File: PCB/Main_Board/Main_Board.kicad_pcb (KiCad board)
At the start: 2 copper layers, 86.9 x 90.9 mm, 26 parts, among them J1 ESP32_Left, J2 ESP32_Right, J3 POWER_SUPPLY, J4 BUCK_IN, J5 BUCK_OUT, J6 CABLE, J7 MOTOR, J8 LIMIT_SWITCH, J9 ToF

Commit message: Minor fixes
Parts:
- J8: renamed from J6; footprint Connector_JST:JST_PH_B8B-PH-K_1x08_P2.00mm_Vertical -> Connector_JST:JST_XH_B8B-XH-A_1x08_P2.50mm_Vertical
- J9: renamed from J7; footprint Connector_JST:JST_PH_B8B-PH-K_1x08_P2.00mm_Vertical -> Connector_JST:JST_XH_B8B-XH-A_1x08_P2.50mm_Vertical
- moved C4 3.81 mm to (78.8, 44.5)
- moved C5 3.81 mm to (90.2, 44.5)
- moved R8 2.54 mm to (86.4, 80.0)
- renumbered C5 to C2, C4 to C3, C3 to C4, C2 to C5, H4 to H1, H3 to H2, H2 to H3, H1 to H4, J3 to J1, J8 to J2, J9 to J3, J1 to J6, J2 to J7, R8 to R1, R5 to R2, R6 to R3, R3 to R4, R4 to R5, R7 to R6, R1 to R7, R2 to R8
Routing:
- net Net-(J8-Pin_7): track 13.1 -> 18.9 mm
- net Net-(J9-Pin_7): track 19.7 -> 23.0 mm
- net /IS_R: track 46.9 -> 50.0 mm
- net Net-(J8-Pin_8): track 23.6 -> 25.9 mm
- net Net-(J8-Pin_4): track 19.8 -> 21.3 mm
- net Net-(J8-Pin_3): track 22.3 -> 23.6 mm
- net Net-(J8-Pin_5): track 7.80 -> 8.89 mm
- net /IS_L: track 53.3 -> 54.4 mm
- net /DISP_RST: track 51.3 -> 50.3 mm
- net Net-(J9-Pin_8): track 8.63 -> 7.82 mm
- net /3V3: track 115.6 -> 114.9 mm
- net /EN_L: track 17.0 -> 17.6 mm
- net /EN_R: track 16.6 -> 17.2 mm
- net /PWM_L: track 17.2 -> 16.7 mm
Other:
- board text added: "ESP32-S3 Meow"

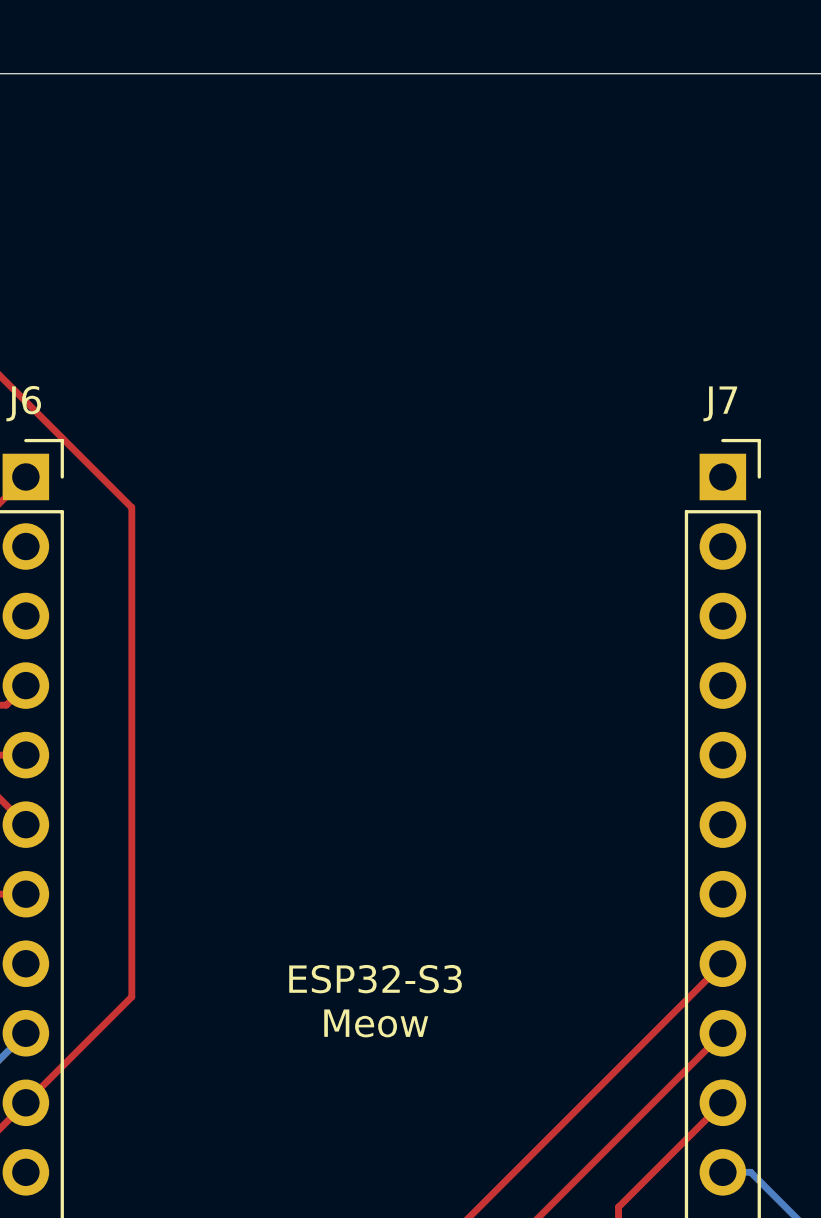
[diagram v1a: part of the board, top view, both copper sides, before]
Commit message: Added UI board Cosmetics in main board
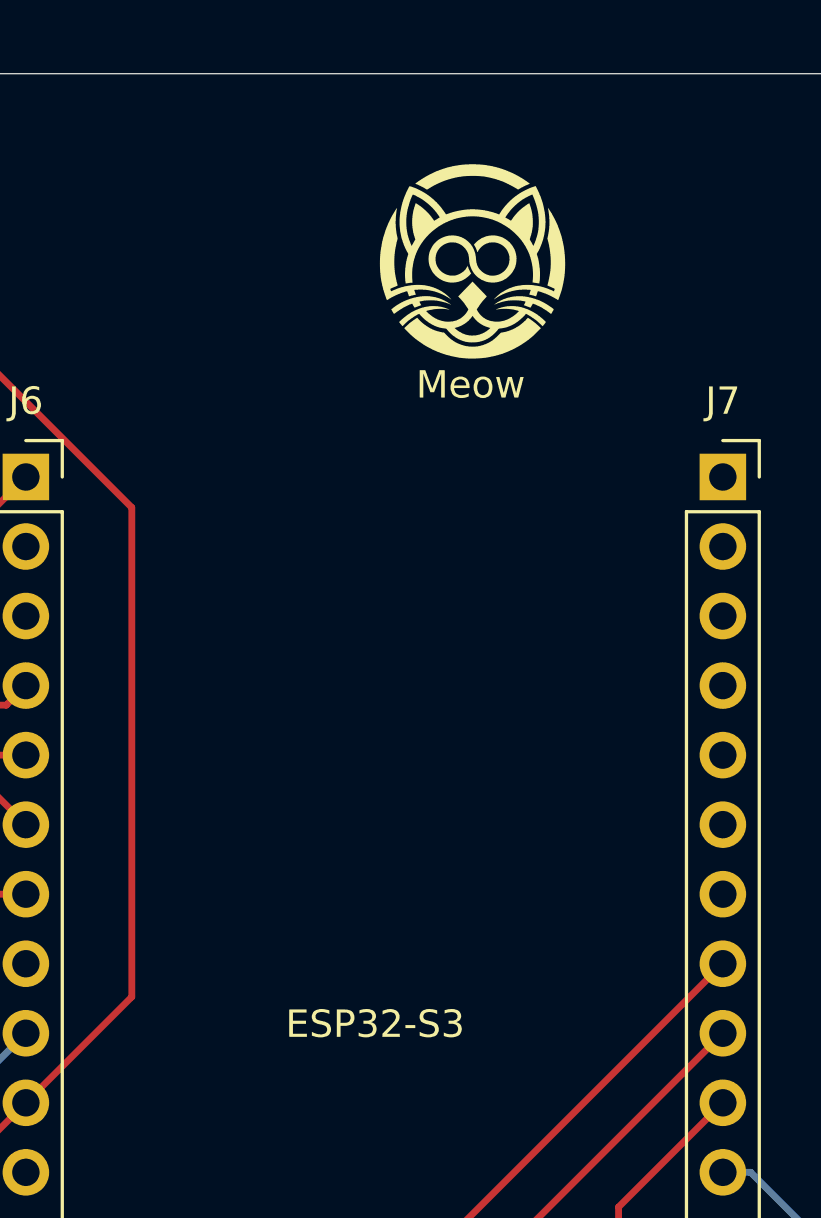
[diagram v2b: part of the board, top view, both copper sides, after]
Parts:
- added ?: , clipboard:13b59317-ab6f-4fc0-bdb4-4b3abb5c9487, F.Cu at (118.2, 43.4)
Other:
- board text added: "ESP32-S3"
- board text added: "Meow"
- board text removed: "ESP32-S3 Meow"

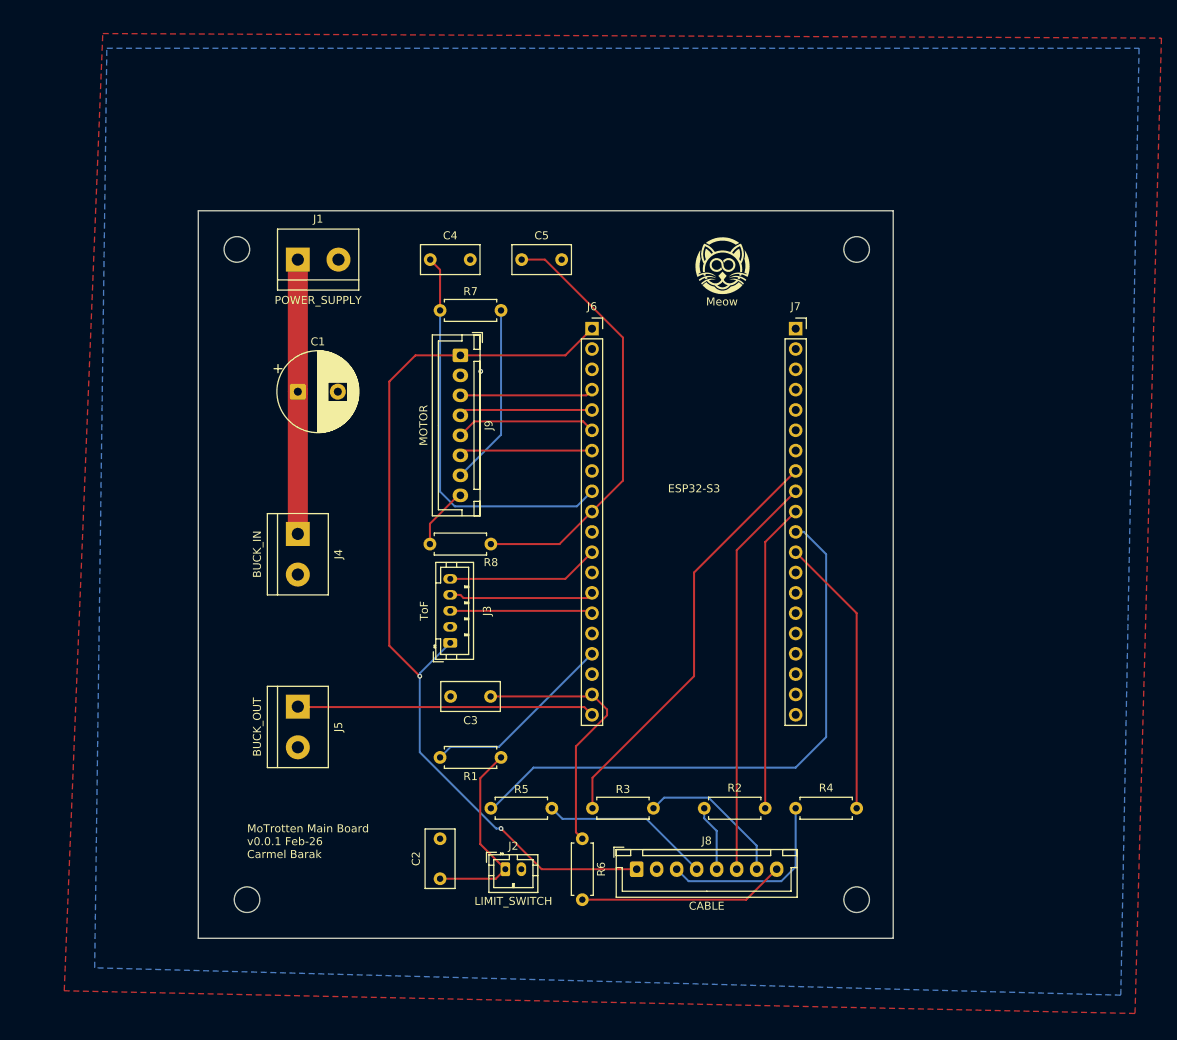
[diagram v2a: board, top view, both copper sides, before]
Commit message: Cleanup main board + fixed GPIOs used
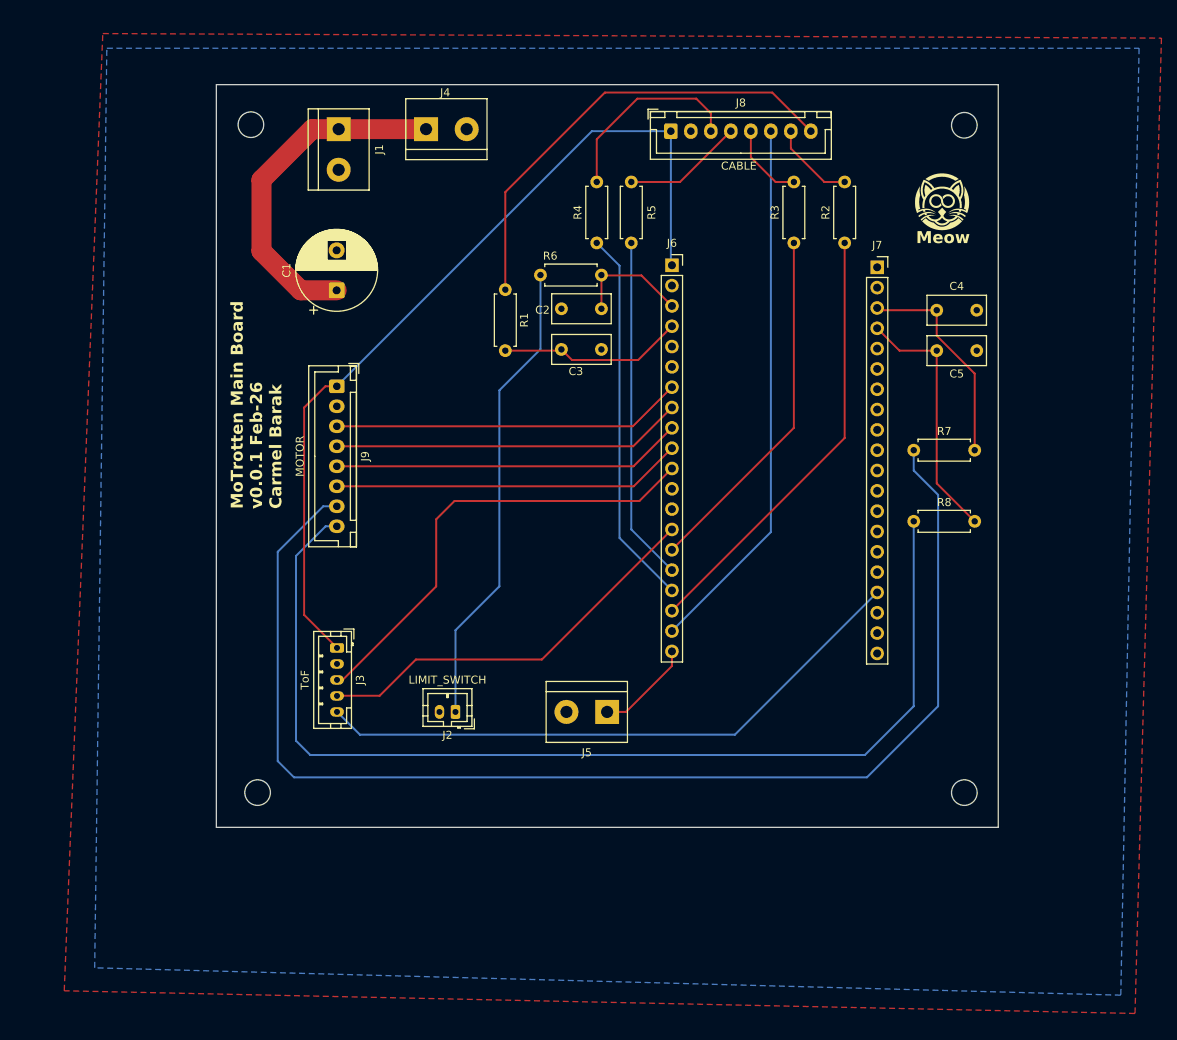
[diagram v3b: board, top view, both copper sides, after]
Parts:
- moved H2 131.9 mm to (145.5, 27.7)
- moved H1 123.0 mm to (56.4, 27.6)
- moved H3 113.5 mm to (145.5, 111.1)
- moved H4 101.1 mm to (57.2, 111.1)
- moved J8 92.4 mm to (108.9, 28.4)
- moved R4 77.8 mm to (99.6, 42.4), turned to 90 degrees
- moved R3 75.0 mm to (124.2, 42.4), turned to 90 degrees
- moved R5 72.8 mm to (103.9, 42.4), turned to 90 degrees
- moved R2 71.4 mm to (130.6, 42.4), turned to 90 degrees
- moved R6 70.7 mm to (92.6, 46.4), turned to 0 degrees
- moved C2 67.9 mm to (95.2, 55.7), turned to 0 degrees
- moved C4 63.6 mm to (142.1, 50.8)
- moved R7 61.7 mm to (139.2, 68.3)
- moved R1 58.5 mm to (88.2, 48.2), turned to -90 degrees
- moved C5 53.1 mm to (142.1, 55.8)
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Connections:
- net Net-(J8-Pin_3) renamed /CLK
- net Net-(J8-Pin_4) renamed /MOSI
- C2 pad 1: /LIMIT_SW -> Net-(J6-Pin_4)
- C3 pad 1: /BTNS -> Net-(J6-Pin_3)
- C4 pad 1: /IS_R -> Net-(J7-Pin_3)
- C5 pad 1: /IS_L -> Net-(J7-Pin_4)
- J6 pad 10: /IS_L -> /EN_L
- J6 pad 11: unconnected-(J6-Pin_11-Pad11) -> /I2C_SDA
- J6 pad 12: /XSHUT -> unconnected-(J6-Pin_12-Pad12)
- J6 pad 15: /I2C_SDA -> /DISP_CS
- J6 pad 16: unconnected-(J6-Pin_16-Pad16) -> /DISP_MOSI
- J6 pad 17: Net-(J6-Pin_17) -> /DISP_CLK
- J6 pad 18: unconnected-(J6-Pin_18-Pad18) -> /DISP_DC
- J6 pad 19: /BTNS -> /DISP_RST
- J6 pad 3: unconnected-(J6-Pin_3-Pad3) -> Net-(J6-Pin_3)
- J6 pad 4: /EN_R -> Net-(J6-Pin_4)
- J6 pad 5: /PWM_R -> unconnected-(J6-Pin_5-Pad5)
- J6 pad 6: /EN_L -> unconnected-(J6-Pin_6-Pad6)
- J6 pad 7: /PWM_L -> /PWM_R
- J6 pad 8: unconnected-(J6-Pin_8-Pad8) -> /PWM_L
- J6 pad 9: /IS_R -> /EN_R
- J7 pad 10: /DISP_DC -> unconnected-(J7-Pin_10-Pad10)
- J7 pad 11: /DISP_CLK -> unconnected-(J7-Pin_11-Pad11)
- J7 pad 12: /DISP_MOSI -> unconnected-(J7-Pin_12-Pad12)
- J7 pad 17: unconnected-(J7-Pin_17-Pad17) -> /XSHUT
- J7 pad 3: unconnected-(J7-Pin_3-Pad3) -> Net-(J7-Pin_3)
- J7 pad 4: unconnected-(J7-Pin_4-Pad4) -> Net-(J7-Pin_4)
- J7 pad 8: /DISP_CS -> unconnected-(J7-Pin_8-Pad8)
- J7 pad 9: /DISP_RST -> unconnected-(J7-Pin_9-Pad9)
- J8 pad 5: Net-(J8-Pin_5) -> /CS
- J8 pad 7: Net-(J8-Pin_7) -> /DC
- J8 pad 8: Net-(J8-Pin_8) -> /BTNS
- J9 pad 3: /EN_R -> /PWM_R
- J9 pad 4: /PWM_R -> /PWM_L
- J9 pad 5: /EN_L -> /EN_R
- J9 pad 6: /PWM_L -> /EN_L
- J9 pad 7: Net-(J9-Pin_7) -> /IS_R
- J9 pad 8: Net-(J9-Pin_8) -> /IS_L
- R1 pad 1: /LIMIT_SW -> /BTNS
- R1 pad 2: Net-(J6-Pin_17) -> Net-(J6-Pin_4)
- R2 pad 2: Net-(J8-Pin_5) -> /DC
- R3 pad 2: Net-(J8-Pin_7) -> /CS
- R4 pad 1: /DISP_MOSI -> /DISP_CLK
- R5 pad 1: /DISP_CLK -> /DISP_MOSI
- R6 pad 1: /BTNS -> /LIMIT_SW
- R6 pad 2: Net-(J8-Pin_8) -> Net-(J6-Pin_3)
- R7 pad 2: Net-(J9-Pin_7) -> Net-(J7-Pin_3)
- R8 pad 2: Net-(J9-Pin_8) -> Net-(J7-Pin_4)
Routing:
- net /IS_R: track 50.0 -> 156.2 mm
- net /IS_L: track 54.4 -> 133.3 mm
- net /XSHUT: track 19.1 -> 76.1 mm
- net /I2C_SDA: track 17.8 -> 57.7 mm
- net /LIMIT_SW: track 25.0 -> 59.0 mm
- net /I2C_SCL: track 17.9 -> 50.5 mm
- net Net-(J7-Pin_4): track 0.00 -> 31.9 mm
- net /PWM_L: track 16.7 -> 43.9 mm
- net /PWM_R: track 16.7 -> 43.9 mm
- net Net-(J7-Pin_3): track 0.00 -> 27.0 mm
- net /EN_R: track 17.2 -> 43.9 mm
- net /EN_L: track 17.6 -> 43.9 mm
- net /DISP_CLK: track 73.5 -> 47.3 mm
- net Net-(J8-Pin_8): track 25.9 -> 0.00 mm
- net /+5V: track 37.2 -> 12.3 mm
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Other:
- board size 86.9 x 90.9 mm -> 97.7 x 92.8 mm
- board text removed: "ESP32-S3"

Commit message: Added fuse + cleanups
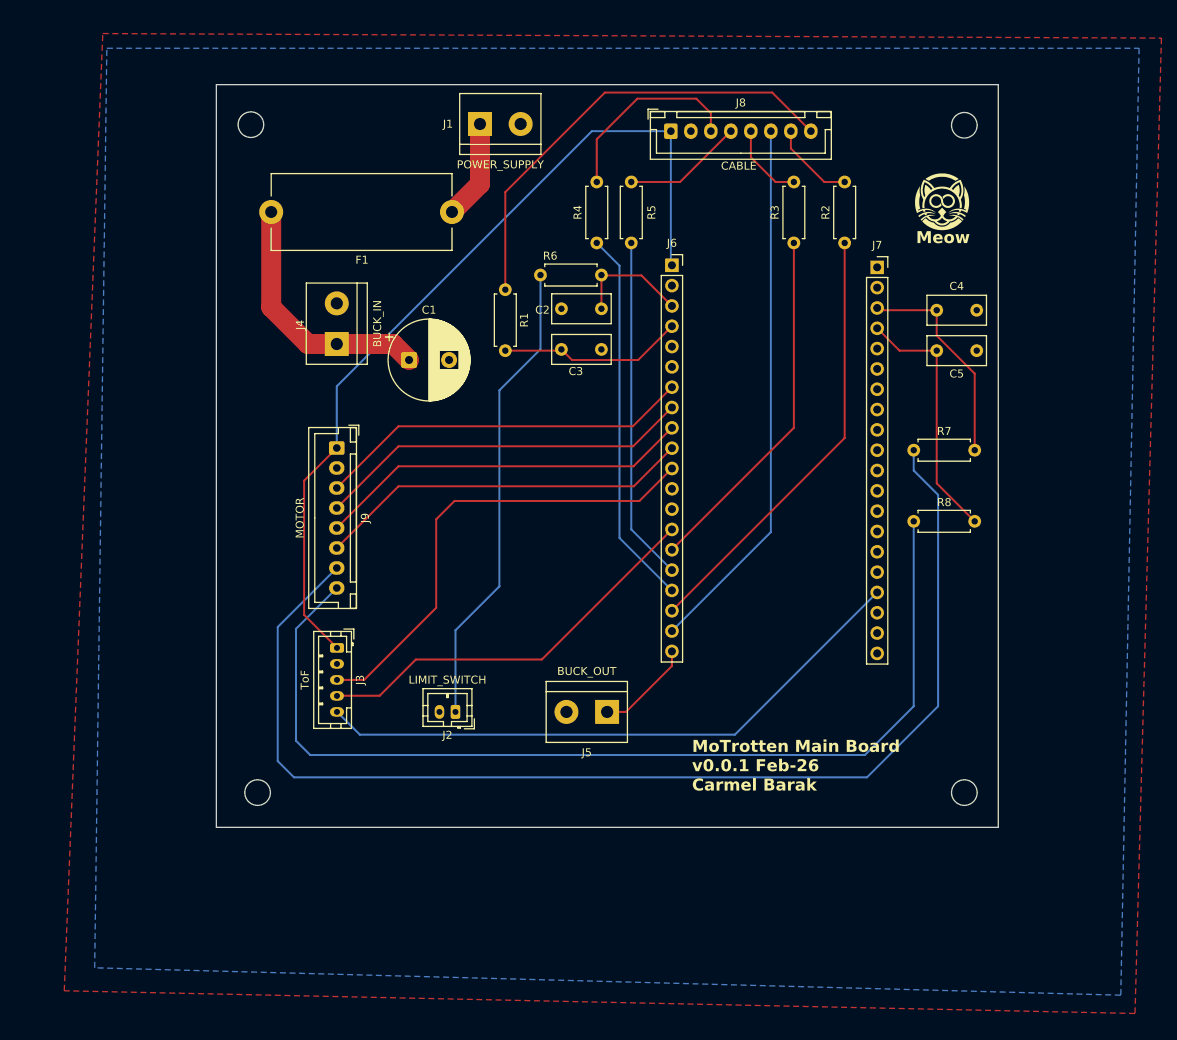
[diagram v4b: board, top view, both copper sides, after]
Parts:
- added F1: Fuse, Fuse:Fuseholder_Cylinder-5x20mm_Stelvio-Kontek_PTF78_Horizontal_Open, F.Cu at (81.5, 38.5)
- moved J4 29.1 mm to (67.1, 55.0), turned to 90 degrees
- moved J1 17.7 mm to (85.0, 27.5), turned to 0 degrees
- moved C1 12.6 mm to (76.1, 57.0), turned to 0 degrees
- moved J9 7.71 mm to (67.1, 68.0)
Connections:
- C1 pad 1: +24V -> /+24VF
- J4 pad 1: +24V -> /+24VF
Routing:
- net /+24VF: track 0.00 -> 31.9 mm
- net +24V: track 43.5 -> 12.4 mm
- net /IS_R: track 156.2 -> 147.5 mm
- net /IS_L: track 133.3 -> 124.8 mm
- net /PWM_R: track 43.9 -> 47.1 mm
- net /EN_R: track 43.9 -> 47.1 mm
- net /EN_L: track 43.9 -> 47.1 mm
- net /PWM_L: track 43.9 -> 47.1 mm
- net /I2C_SDA: track 57.7 -> 60.0 mm
- net /3V3: track 108.7 -> 107.9 mm

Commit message: Updated boards and added DRU files
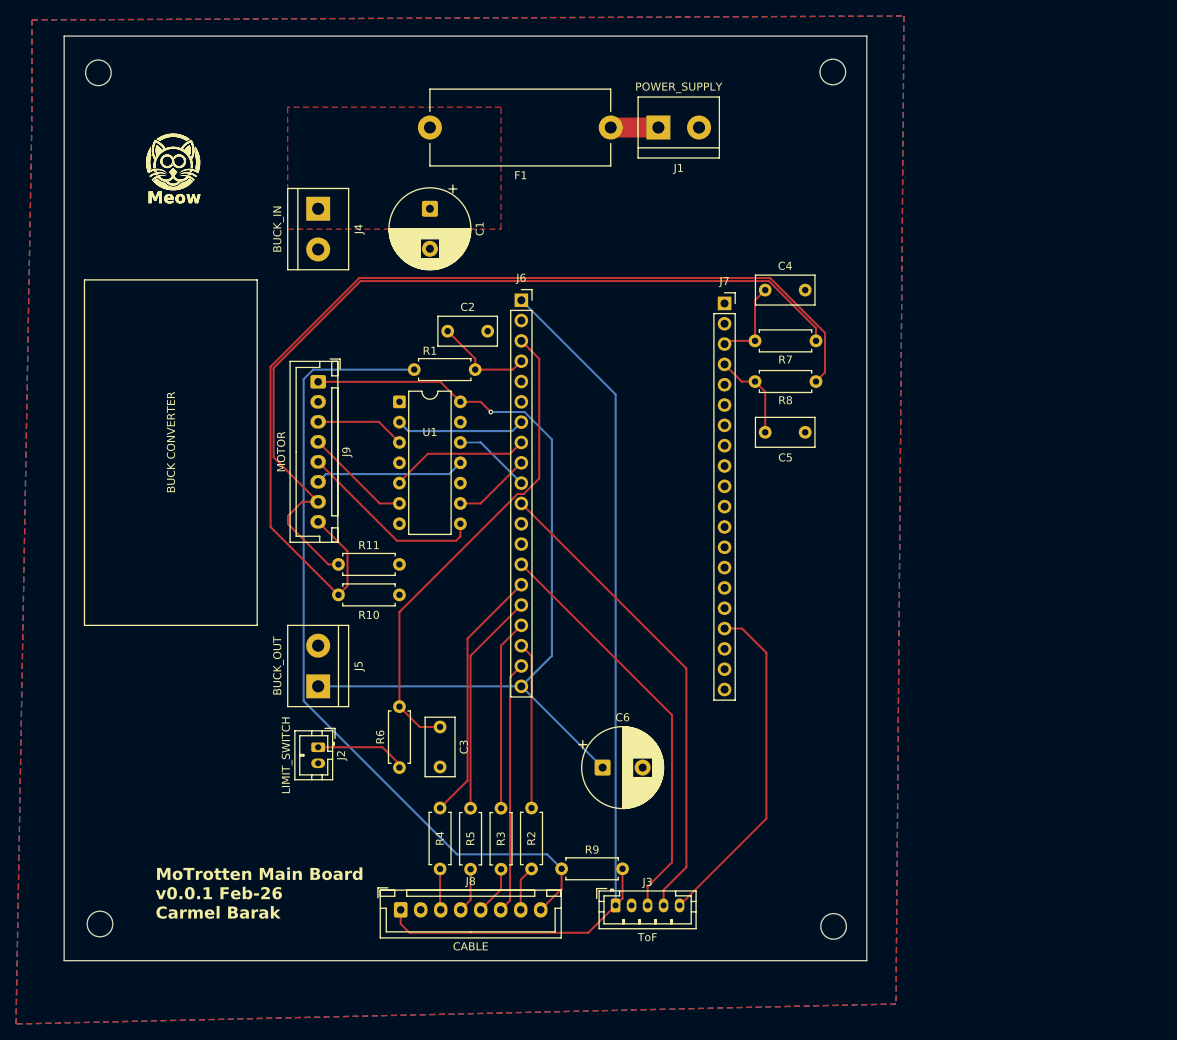
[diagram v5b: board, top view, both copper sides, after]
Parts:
- removed the ? at (145.6, 35.5)
- added ? (x2): , clipboard:13b59317-ab6f-4fc0-bdb4-4b3abb5c9487, F.Cu at (49.5, 30.5)
- added C6: 470uF, Capacitor_THT:CP_Radial_D10.0mm_P5.00mm, F.Cu at (100.3, 108.0)
- added R10: 1K, Resistor_THT:R_Axial_DIN0207_L6.3mm_D2.5mm_P7.62mm_Horizontal, F.Cu at (67.3, 86.4)
- added R11: 1K, Resistor_THT:R_Axial_DIN0207_L6.3mm_D2.5mm_P7.62mm_Horizontal, F.Cu at (67.3, 82.5)
- added R9: 10K, Resistor_THT:R_Axial_DIN0207_L6.3mm_D2.5mm_P7.62mm_Horizontal, F.Cu at (95.2, 120.6)
- added U1: 74AHCT125, Package_DIP:DIP-14_W7.62mm, F.Cu at (74.9, 62.2)
- moved H3 109.3 mm to (37.5, 127.5)
- moved J8 103.0 mm to (75.1, 125.7)
- moved H2 101.5 mm to (129.2, 127.8)
- moved H4 92.1 mm to (37.3, 21.1)
- moved R2 80.8 mm to (91.4, 113.0), turned to -90 degrees
- moved R3 79.6 mm to (87.6, 113.0), turned to -90 degrees
- moved R5 73.5 mm to (83.8, 113.0), turned to -90 degrees
- moved R4 73.3 mm to (80.0, 113.0), turned to -90 degrees
- moved H1 73.0 mm to (129.1, 21.0)
- moved R6 64.0 mm to (74.9, 108.0), turned to 90 degrees
- moved C3 56.0 mm to (80.0, 102.9), turned to -90 degrees
- moved J3 47.4 mm to (102.0, 125.2), turned to 0 degrees
- moved J5 36.3 mm to (64.8, 97.8), turned to 90 degrees
- moved C5 23.7 mm to (120.7, 66.0)
- moved F1 22.5 mm to (101.3, 27.9)
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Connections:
- J3 pad 3: /I2C_SDA -> /I2C_SCL
- J3 pad 4: /I2C_SCL -> /I2C_SDA
- J6 pad 10: /EN_L -> /EN_L_3V3
- J6 pad 7: /PWM_R -> /PWM_R_3V3
- J6 pad 8: /PWM_L -> /PWM_L_3V3
- J6 pad 9: /EN_R -> /EN_R_3V3
- J8 pad 3: /CLK -> /CS
- J8 pad 5: /CS -> /CLK
- J9 pad 1: /3V3 -> /+5V
- R3 pad 1: /DISP_CS -> /DISP_CLK
- R3 pad 2: /CS -> /CLK
- R4 pad 1: /DISP_CLK -> /DISP_CS
- R4 pad 2: /CLK -> /CS
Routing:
- net /+5V: track 12.3 -> 104.7 mm, vias 0 -> 1
- net /LIMIT_SW: track 59.0 -> 11.8 mm
- net Net-(J6-Pin_3): track 14.6 -> 60.5 mm
- net /BTNS: track 57.5 -> 101.7 mm
- net /IS_R: track 147.5 -> 109.3 mm
- net /DISP_RST: track 67.6 -> 31.5 mm
- net /PWM_R: track 47.1 -> 11.2 mm
- net /DISP_DC: track 54.9 -> 20.8 mm
- net /PWM_L: track 47.1 -> 13.3 mm
- net /XSHUT: track 76.1 -> 42.6 mm
- net /+24VF: track 31.9 -> 0.00 mm
- net /EN_L: track 47.1 -> 18.8 mm
- net /DISP_CLK: track 47.3 -> 23.9 mm
- net /EN_R: track 47.1 -> 23.7 mm
- net Net-(J7-Pin_4): track 31.9 -> 11.6 mm
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- added copper zone on F.Cu, net /+24VF
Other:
- board size 97.7 x 92.8 mm -> 100.3 x 115.6 mm
- board text added: "BUCK CONVERTER"
